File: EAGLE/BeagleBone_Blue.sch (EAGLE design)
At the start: 299 parts, among them J2 STRAWSON_EAGLE_LIB_SERVO_HEAD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, M1 JST_ZH_2, M2 JST_ZH_2, M3 JST_ZH_2, M4 JST_ZH_2, Q1 MOSFET-N, U1 TCAN1051HV, U10 TXS0108ERGYR, U13 EMMC, U2 SN74LV1T126DBVR, U3 TPD4S012DRY, U4 TPD4S012DRY, U5 24LC_32AT-I/OT, U6 SN74LVC1G07_DCK_5, U7 WL1835MODGBMOCT, U8 TPS2105_DBV_5, U9 TXS0108ERGYR, X2 SCHA5B0200, X3 USB1, X4 10118192-0001LF, Y1 24 MHz, Y2 32.768kHz

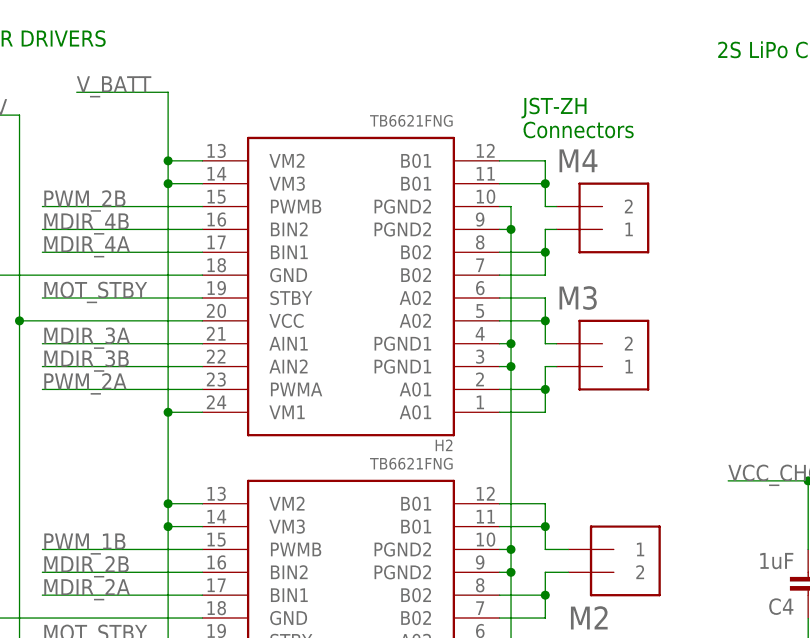
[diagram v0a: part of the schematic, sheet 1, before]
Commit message: Issue #8 Motor driver chip is mislabelled EAGLE
A global search and replace s/TB6621FNG/TB6612FNG/g of
the eagle files.
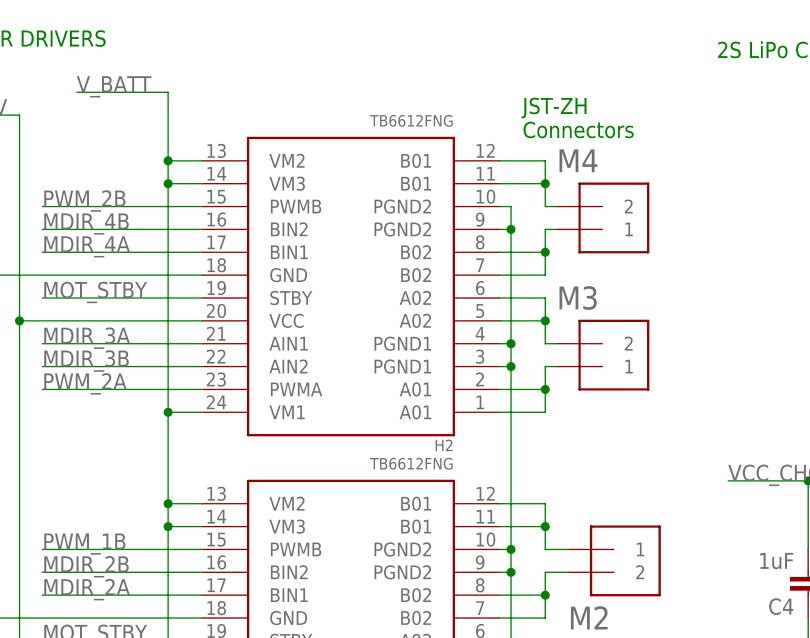
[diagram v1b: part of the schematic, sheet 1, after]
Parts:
- H1, H2: value TB6621FNG -> TB6612FNG; device SparkFun:TB6621FNG -> SparkFun:TB6612FNG
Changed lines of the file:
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@@
 </classes>
 <parts>
-<part name="H1" library="SparkFun" deviceset="TB6621FNG" device=""/>
+<part name="H1" library="SparkFun" deviceset="TB6612FNG" device=""/>
 <part name="C2" library="Strawson_Eagle_Lib" deviceset="CAP" device="0402-CAP" value="0.1uF"/>
-<part name="H2" library="SparkFun" deviceset="TB6621FNG" device=""/>
+<part name="H2" library="SparkFun" deviceset="TB6612FNG" device=""/>
 <part name="GND16" library="SparkFun-Aesthetics" deviceset="GND" device=""/>
 <part name="GND18" library="SparkFun" deviceset="GND" device=""/>
